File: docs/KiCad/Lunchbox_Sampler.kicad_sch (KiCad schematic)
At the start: 48 parts, among them J1 Conn_01x14_MountingPin, J10 Conn_01x02, J11 NMJ4HCD2, J16 NMJ4HCD2, J17 NMJ4HCD2, J18 NMJ4HCD2, J2 Conn_01x14_MountingPin, J3 DIN-5, J4 06JQ-BT, J5 Conn_01x07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

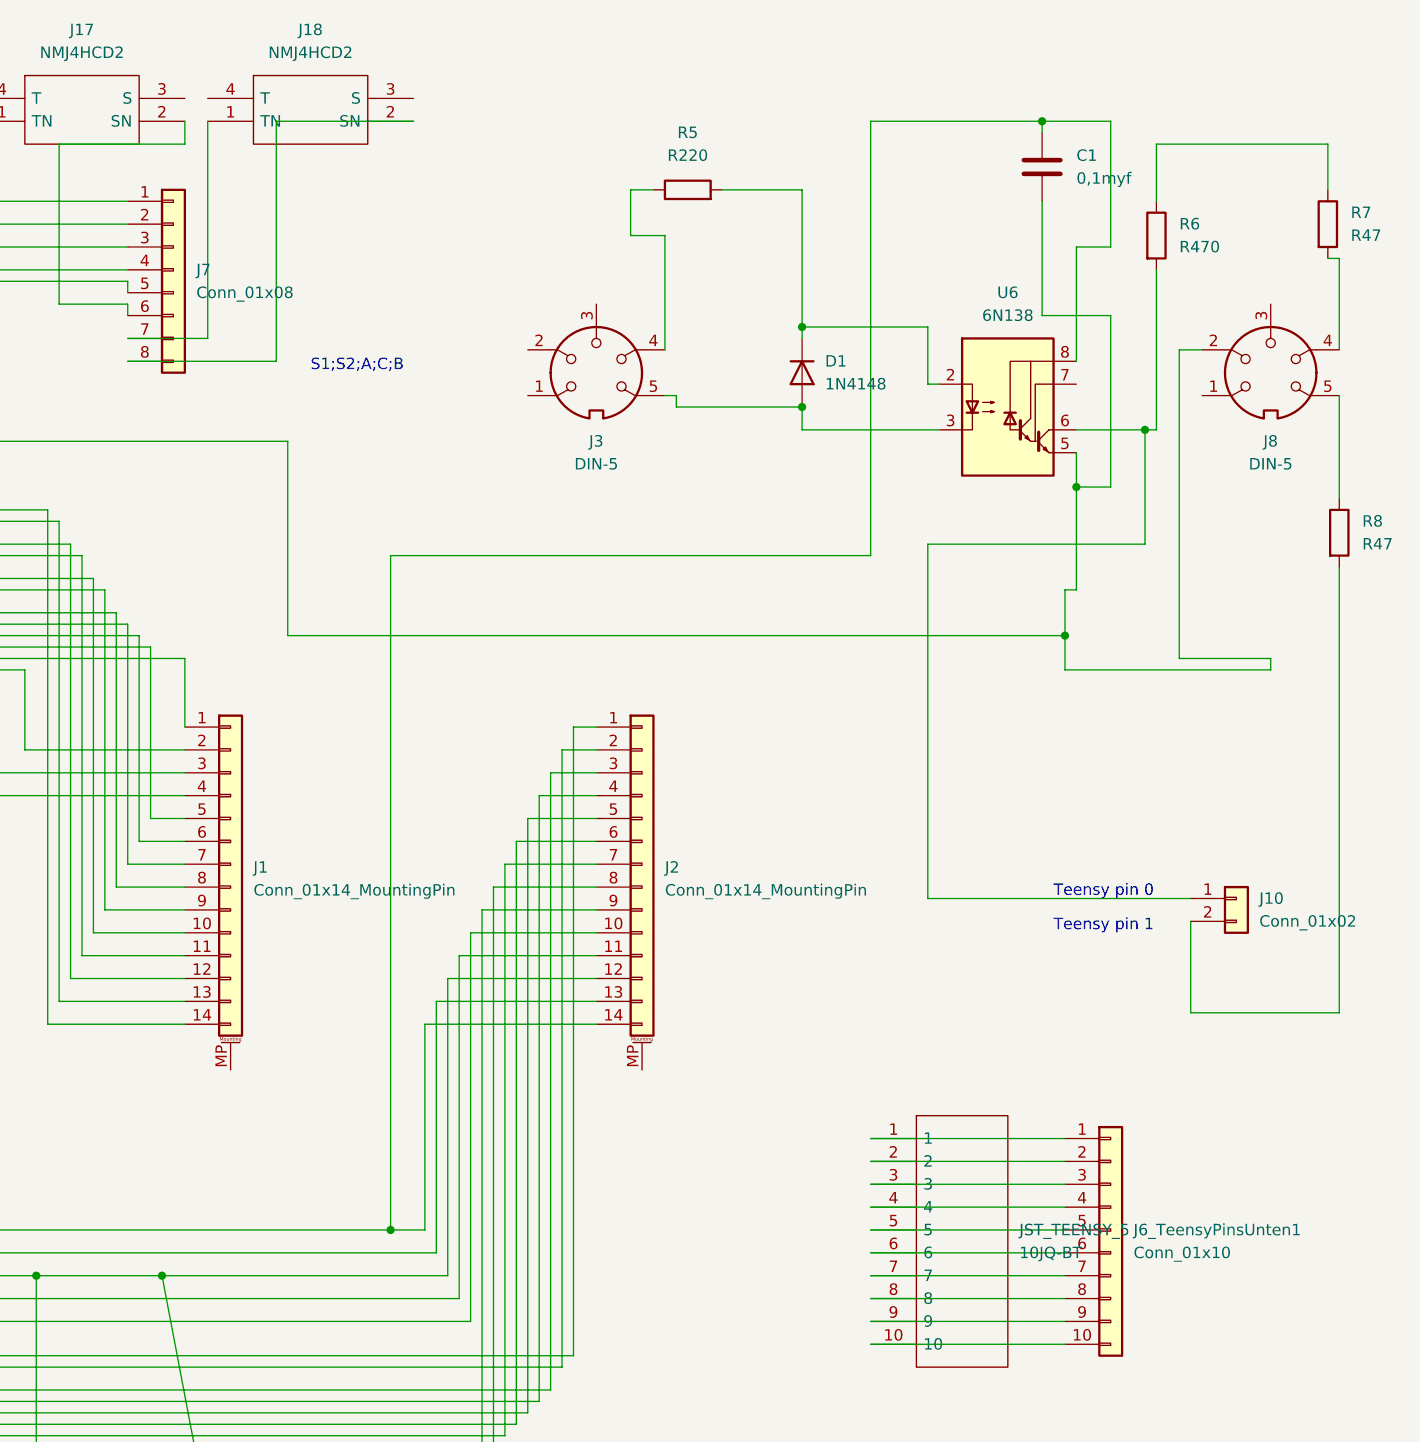
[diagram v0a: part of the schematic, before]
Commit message: structured and added interactive tests, updated KiCad files
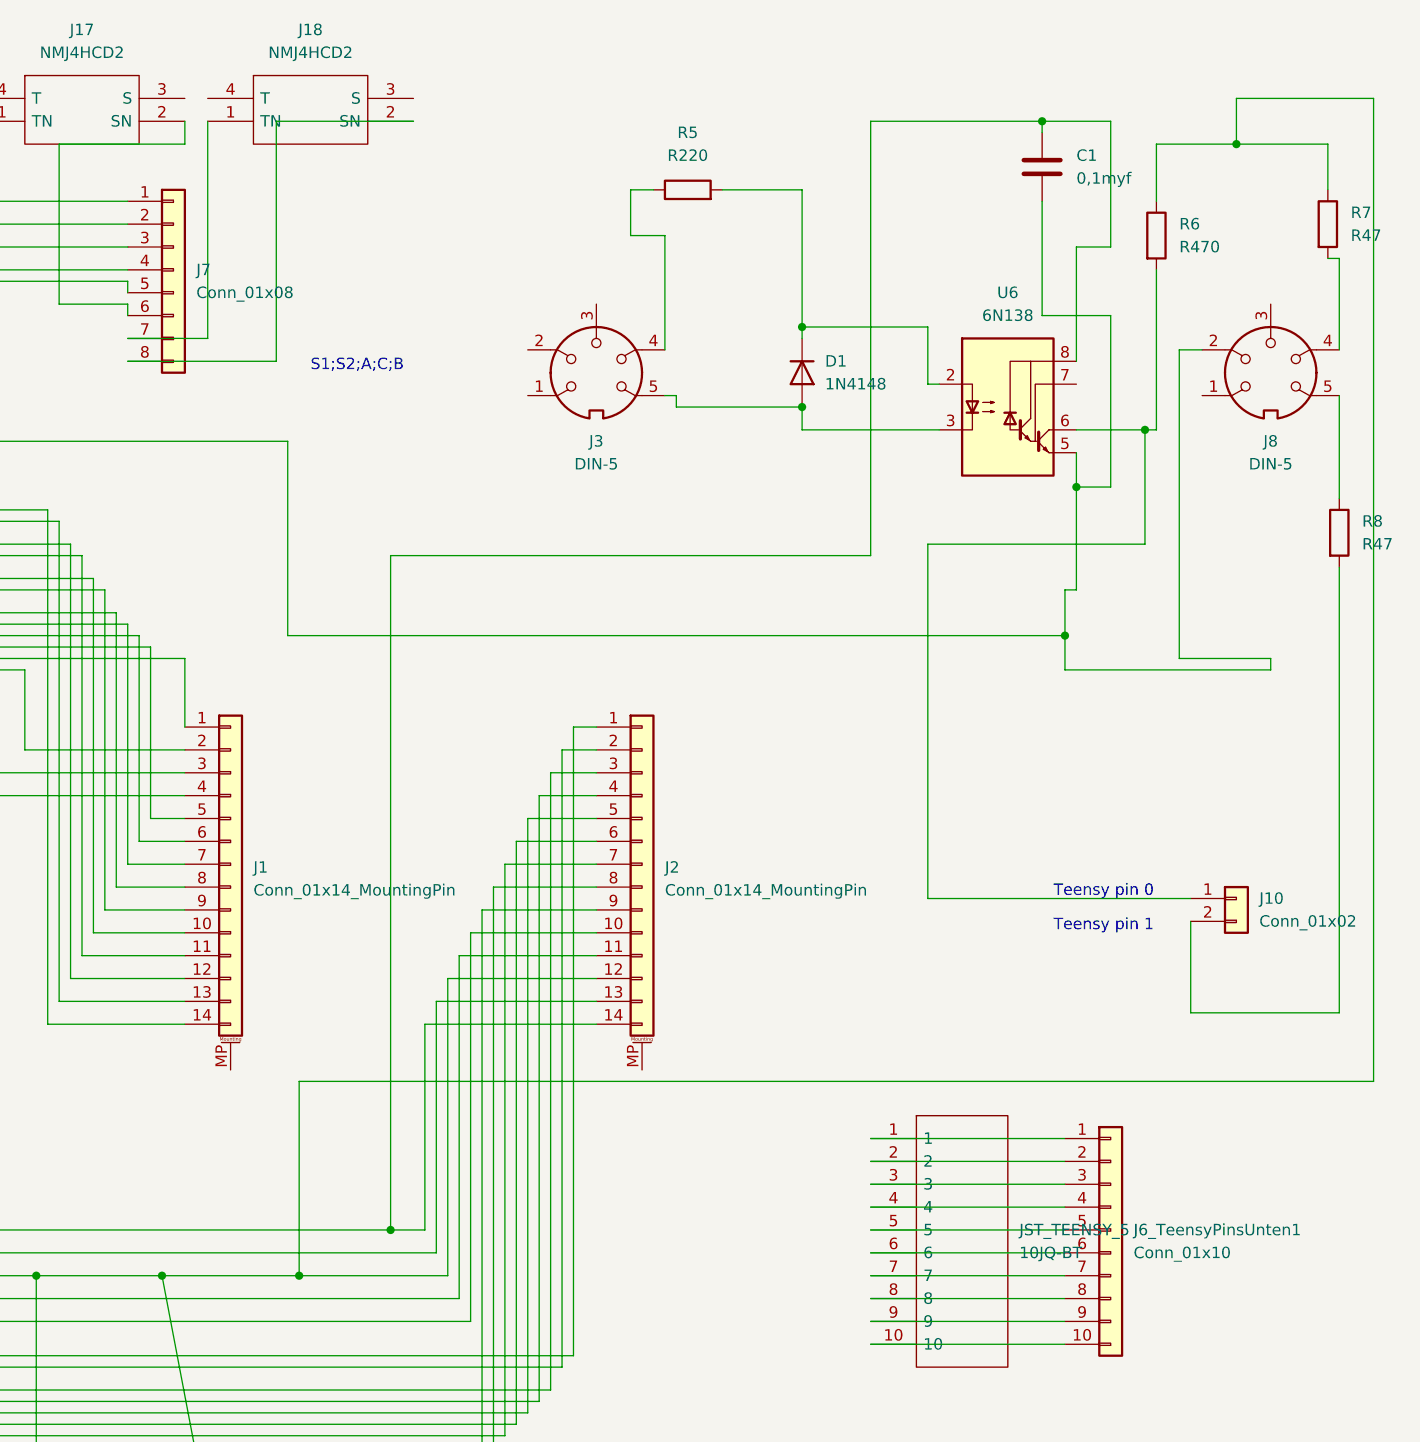
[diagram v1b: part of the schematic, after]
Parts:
- J4, J?3=FSR4;6=FSR1: footprint (none) -> Connector_JST:JST_XH_B6B-XH-A_1x06_P2.50mm_Vertical
- R1, R2, R3, R4, R5, R6, R7, R8: footprint Resistor_THT:R_Axial_DIN0411_L9.9mm_D3.6mm_P7.62mm_Vertical -> (none)
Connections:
- net at R6.1, R7.1: now also J2.12 (Pin_12), J4.2, U5.16 (VCC), U7.31 (3V3)
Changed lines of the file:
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@@
   (junction (at 16.51 198.12) (diameter 0) (color 0 0 0 0)
   )
+  (junction (at 281.94 147.32) (diameter 0) (color 0 0 0 0)
+  )
   (junction (at 337.82 50.8) (diameter 0) (color 0 0 0 0)
   )
@@
   (junction (at 375.92 53.34) (diameter 0) (color 0 0 0 0)
   )
+  (junction (at 386.08 21.59) (diameter 0) (color 0 0 0 0)
+  )
   (junction (at 73.66 191.77) (diameter 0) (color 0 0 0 0)
   )
@@
     (stroke (width 0) (type default) (color 0 0 0 0))
   )
+  (wire (pts (xy 401.32 16.51) (xy 401.32 125.73))
+    (stroke (width 0) (type default) (color 0 0 0 0))
+  )
   (wire (pts (xy 180.34 139.7) (xy 175.26 139.7))
     (stroke (width 0) (type default) (color 0 0 0 0))
@@
     (stroke (width 0) (type default) (color 0 0 0 0))
   )
+  (wire (pts (xy 281.94 147.32) (xy 298.45 147.32))
+    (stroke (width 0) (type default) (color 0 0 0 0))
+  )
   (wire (pts (xy 364.49 19.05) (xy 372.11 19.05))
     (stroke (width 0) (type default) (color 0 0 0 0))
@@
     (stroke (width 0) (type default) (color 0 0 0 0))
   )
+  (wire (pts (xy 401.32 125.73) (xy 281.94 125.73))
+    (stroke (width 0) (type default) (color 0 0 0 0))
+  )
   (wire (pts (xy 243.84 144.78) (xy 297.18 144.78))
     (stroke (width 0) (type default) (color 0 0 0 0))
@@
     (stroke (width 0) (type default) (color 0 0 0 0))
   )
-  (wire (pts (xy 266.7 147.32) (xy 298.45 147.32))
-    (stroke (width 0) (type default) (color 0 0 0 0))
-  )
-  (wire (pts (xy 377.19 21.59) (xy 396.24 21.59))
+  (wire (pts (xy 266.7 147.32) (xy 281.94 147.32))
+    (stroke (width 0) (type default) (color 0 0 0 0))
+  )
+  (wire (pts (xy 377.19 21.59) (xy 386.08 21.59))
     (stroke (width 0) (type default) (color 0 0 0 0))
   )
@@
     (stroke (width 0) (type default) (color 0 0 0 0))
   )
+  (wire (pts (xy 386.08 21.59) (xy 396.24 21.59))
+    (stroke (width 0) (type default) (color 0 0 0 0))
+  )
   (wire (pts (xy 242.57 199.39) (xy 261.62 199.39))
     (stroke (width 0) (type default) (color 0 0 0 0))
@@
     (stroke (width 0) (type default) (color 0 0 0 0))
   )
+  (wire (pts (xy 386.08 21.59) (xy 386.08 16.51))
+    (stroke (width 0) (type default) (color 0 0 0 0))
+  )
   (wire (pts (xy 269.24 86.36) (xy 269.24 78.74))
     (stroke (width 0) (type default) (color 0 0 0 0))
@@
     (stroke (width 0) (type default) (color 0 0 0 0))
   )
+  (wire (pts (xy 386.08 16.51) (xy 401.32 16.51))
+    (stroke (width 0) (type default) (color 0 0 0 0))
+  )
   (wire (pts (xy 95.25 200.66) (xy 118.11 200.66))
     (stroke (width 0) (type default) (color 0 0 0 0))
@@
   )
   (wire (pts (xy 99.06 125.73) (xy 96.52 125.73))
+    (stroke (width 0) (type default) (color 0 0 0 0))
+  )
+  (wire (pts (xy 281.94 125.73) (xy 281.94 147.32))
     (stroke (width 0) (type default) (color 0 0 0 0))
   )
@@
       (effects (font (size 1.27 1.27)) (justify left))
     )
-    (property "Footprint" "Resistor_THT:R_Axial_DIN0411_L9.9mm_D3.6mm_P7.62mm_Vertical" (id 2) (at 126.492 160.02 90)
+    (property "Footprint" "" (id 2) (at 126.492 160.02 90)
       (effects (font (size 1.27 1.27)) hide)
     )
@@
       (effects (font (size 1.27 1.27)) (justify left))
     )
-    (property "Footprint" "" (id 2) (at 134.62 209.55 0)
+    (property "Footprint" "Connector_JST:JST_XH_B6B-XH-A_1x06_P2.50mm_Vertical" (id 2) (at 134.62 209.55 0)
       (effects (font (size 1.27 1.27)) (justify left) hide)
     )
@@
       (effects (font (size 1.27 1.27)) (justify left))
     )
-    (property "Footprint" "Resistor_THT:R_Axial_DIN0411_L9.9mm_D3.6mm_P7.62mm_Vertical" (id 2) (at 375.412 31.75 90)
+    (property "Footprint" "" (id 2) (at 375.412 31.75 90)
       (effects (font (size 1.27 1.27)) hide)
     )
@@
       (effects (font (size 1.27 1.27)) (justify left))
     )
-    (property "Footprint" "Resistor_THT:R_Axial_DIN0411_L9.9mm_D3.6mm_P7.62mm_Vertical" (id 2) (at 126.492 181.61 90)
+    (property "Footprint" "" (id 2) (at 126.492 181.61 90)
       (effects (font (size 1.27 1.27)) hide)
     )
@@
     (property "Reference" "R5" (id 0) (at 325.12 20.32 90))
     (property "Value" "R220" (id 1) (at 325.12 22.86 90))
-    (property "Footprint" "Resistor_THT:R_Axial_DIN0411_L9.9mm_D3.6mm_P7.62mm_Vertical" (id 2) (at 325.12 28.448 90)
+    (property "Footprint" "" (id 2) (at 325.12 28.448 90)
       (effects (font (size 1.27 1.27)) hide)
     )
@@
       (effects (font (size 1.27 1.27)) (justify left))
     )
-    (property "Footprint" "" (id 2) (at 278.13 184.15 0)
+    (property "Footprint" "Connector_JST:JST_XH_B6B-XH-A_1x06_P2.50mm_Vertical" (id 2) (at 278.13 184.15 0)
       (effects (font (size 1.27 1.27)) (justify left) hide)
     )
@@
       (effects (font (size 1.27 1.27)) (justify left))
     )
-    (property "Footprint" "Resistor_THT:R_Axial_DIN0411_L9.9mm_D3.6mm_P7.62mm_Vertical" (id 2) (at 395.732 64.77 90)
+    (property "Footprint" "" (id 2) (at 395.732 64.77 90)
       (effects (font (size 1.27 1.27)) hide)
     )
@@
       (effects (font (size 1.27 1.27)) (justify left))
     )
-    (property "Footprint" "Resistor_THT:R_Axial_DIN0411_L9.9mm_D3.6mm_P7.62mm_Vertical" (id 2) (at 394.462 30.48 90)
+    (property "Footprint" "" (id 2) (at 394.462 30.48 90)
       (effects (font (size 1.27 1.27)) hide)
     )
@@
       (effects (font (size 1.27 1.27)) (justify left))
     )
-    (property "Footprint" "Resistor_THT:R_Axial_DIN0411_L9.9mm_D3.6mm_P7.62mm_Vertical" (id 2) (at 50.292 180.34 90)
+    (property "Footprint" "" (id 2) (at 50.292 180.34 90)
       (effects (font (size 1.27 1.27)) hide)
     )
@@
       (effects (font (size 1.27 1.27)) (justify left))
     )
-    (property "Footprint" "Resistor_THT:R_Axial_DIN0411_L9.9mm_D3.6mm_P7.62mm_Vertical" (id 2) (at 52.832 147.32 90)
+    (property "Footprint" "" (id 2) (at 52.832 147.32 90)
       (effects (font (size 1.27 1.27)) hide)
     )
@@
     )
     (path "/c2f40f12-9140-473b-8e1d-752c1c930d8b"
-      (reference "R1") (unit 1) (value "R_Variable") (footprint "Resistor_THT:R_Axial_DIN0411_L9.9mm_D3.6mm_P7.62mm_Vertical")
+      (reference "R1") (unit 1) (value "R_Variable") (footprint "Resistor_THT:R_Axial_DIN0411_L9.9mm_D3.6mm_P12.70mm_Horizontal")
     )
     (path "/ebdccc38-546b-4d29-8a1d-1ab8adf77e08"
-      (reference "R2") (unit 1) (value "R_Variable") (footprint "Resistor_THT:R_Axial_DIN0411_L9.9mm_D3.6mm_P7.62mm_Vertical")
+      (reference "R2") (unit 1) (value "R_Variable") (footprint "Resistor_THT:R_Axial_DIN0411_L9.9mm_D3.6mm_P12.70mm_Horizontal")
     )
     (path "/0e6aea34-c909-43eb-ab34-679ff8f629ea"
-      (reference "R3") (unit 1) (value "R_Variable") (footprint "Resistor_THT:R_Axial_DIN0411_L9.9mm_D3.6mm_P7.62mm_Vertical")
+      (reference "R3") (unit 1) (value "R_Variable") (footprint "Resistor_THT:R_Axial_DIN0411_L9.9mm_D3.6mm_P12.70mm_Horizontal")
     )
     (path "/3a878acd-db72-4060-9445-ca901d7fd684"
-      (reference "R4") (unit 1) (value "R_Variable") (footprint "Resistor_THT:R_Axial_DIN0411_L9.9mm_D3.6mm_P7.62mm_Vertical")
+      (reference "R4") (unit 1) (value "R_Variable") (footprint "Resistor_THT:R_Axial_DIN0411_L9.9mm_D3.6mm_P12.70mm_Horizontal")
     )
     (path "/4ed70811-c8d4-4de3-9055-2b61827964a3"
-      (reference "R5") (unit 1) (value "R220") (footprint "Resistor_THT:R_Axial_DIN0411_L9.9mm_D3.6mm_P7.62mm_Vertical")
+      (reference "R5") (unit 1) (value "R220") (footprint "Resistor_THT:R_Axial_DIN0411_L9.9mm_D3.6mm_P12.70mm_Horizontal")
     )
     (path "/275c3e87-6b92-4445-ae44-835199568f46"
-      (reference "R6") (unit 1) (value "R470") (footprint "Resistor_THT:R_Axial_DIN0411_L9.9mm_D3.6mm_P7.62mm_Vertical")
+      (reference "R6") (unit 1) (value "R470") (footprint "Resistor_THT:R_Axial_DIN0411_L9.9mm_D3.6mm_P12.70mm_Horizontal")
     )
     (path "/a55421f9-e4b3-4b95-9a5c-a833b0f7321f"
-      (reference "R7") (unit 1) (value "R47") (footprint "Resistor_THT:R_Axial_DIN0411_L9.9mm_D3.6mm_P7.62mm_Vertical")
+      (reference "R7") (unit 1) (value "R47") (footprint "Resistor_THT:R_Axial_DIN0411_L9.9mm_D3.6mm_P12.70mm_Horizontal")
     )
     (path "/8a532a5e-bef9-4902-a8e4-8351de1e5086"
-      (reference "R8") (unit 1) (value "R47") (footprint "Resistor_THT:R_Axial_DIN0411_L9.9mm_D3.6mm_P7.62mm_Vertical")
+      (reference "R8") (unit 1) (value "R47") (footprint "Resistor_THT:R_Axial_DIN0411_L9.9mm_D3.6mm_P12.70mm_Horizontal")
     )
     (path "/968876f6-82e7-4e81-aa4a-d5e5e11ed1a1"
